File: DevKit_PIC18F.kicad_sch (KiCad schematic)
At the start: 27 parts, among them J1 PIC_ICSP_ICD, J2 USB_C_Receptacle_USB2.0_16P, J4 RA_PORT, J5 RB_PORT, J6 RD_PORT, J7 RC_PORT, J8 RE_PORT, J9 2P_UART, SW1 SW_DIP, X1 16MHz

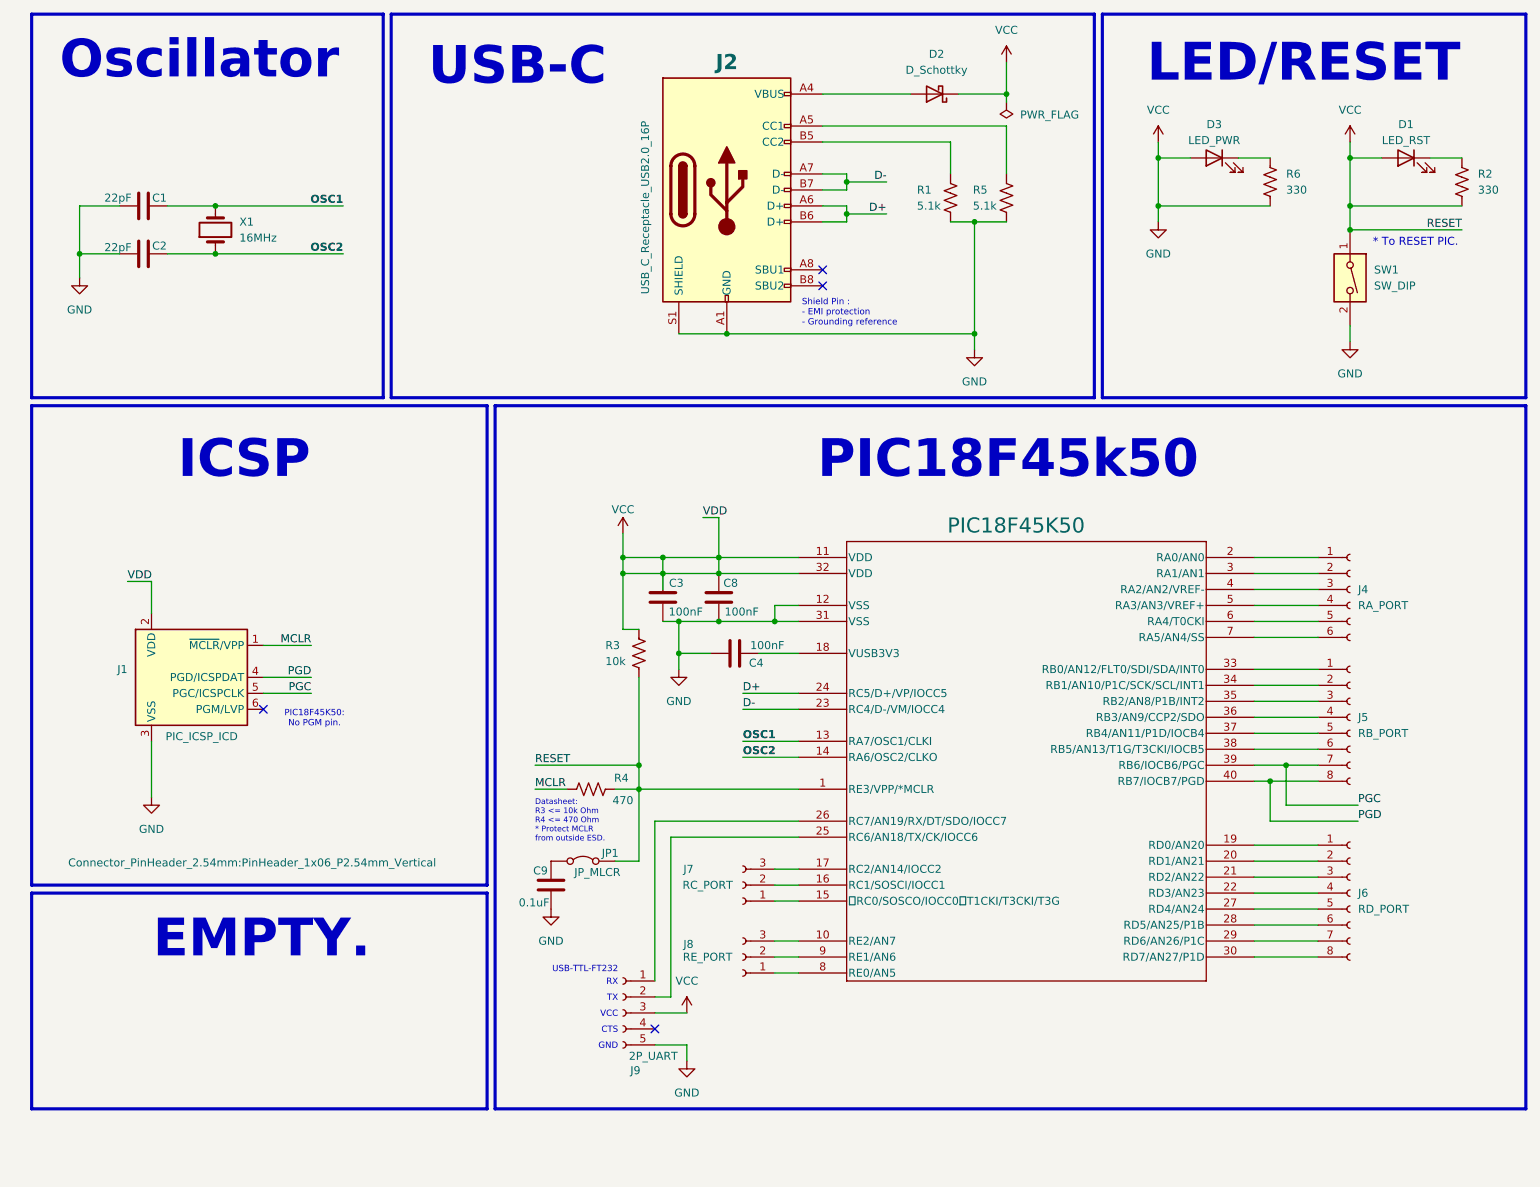
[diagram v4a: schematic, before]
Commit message: Added ICSP LED, D+/- tuned length, Cap placement/footprint update.
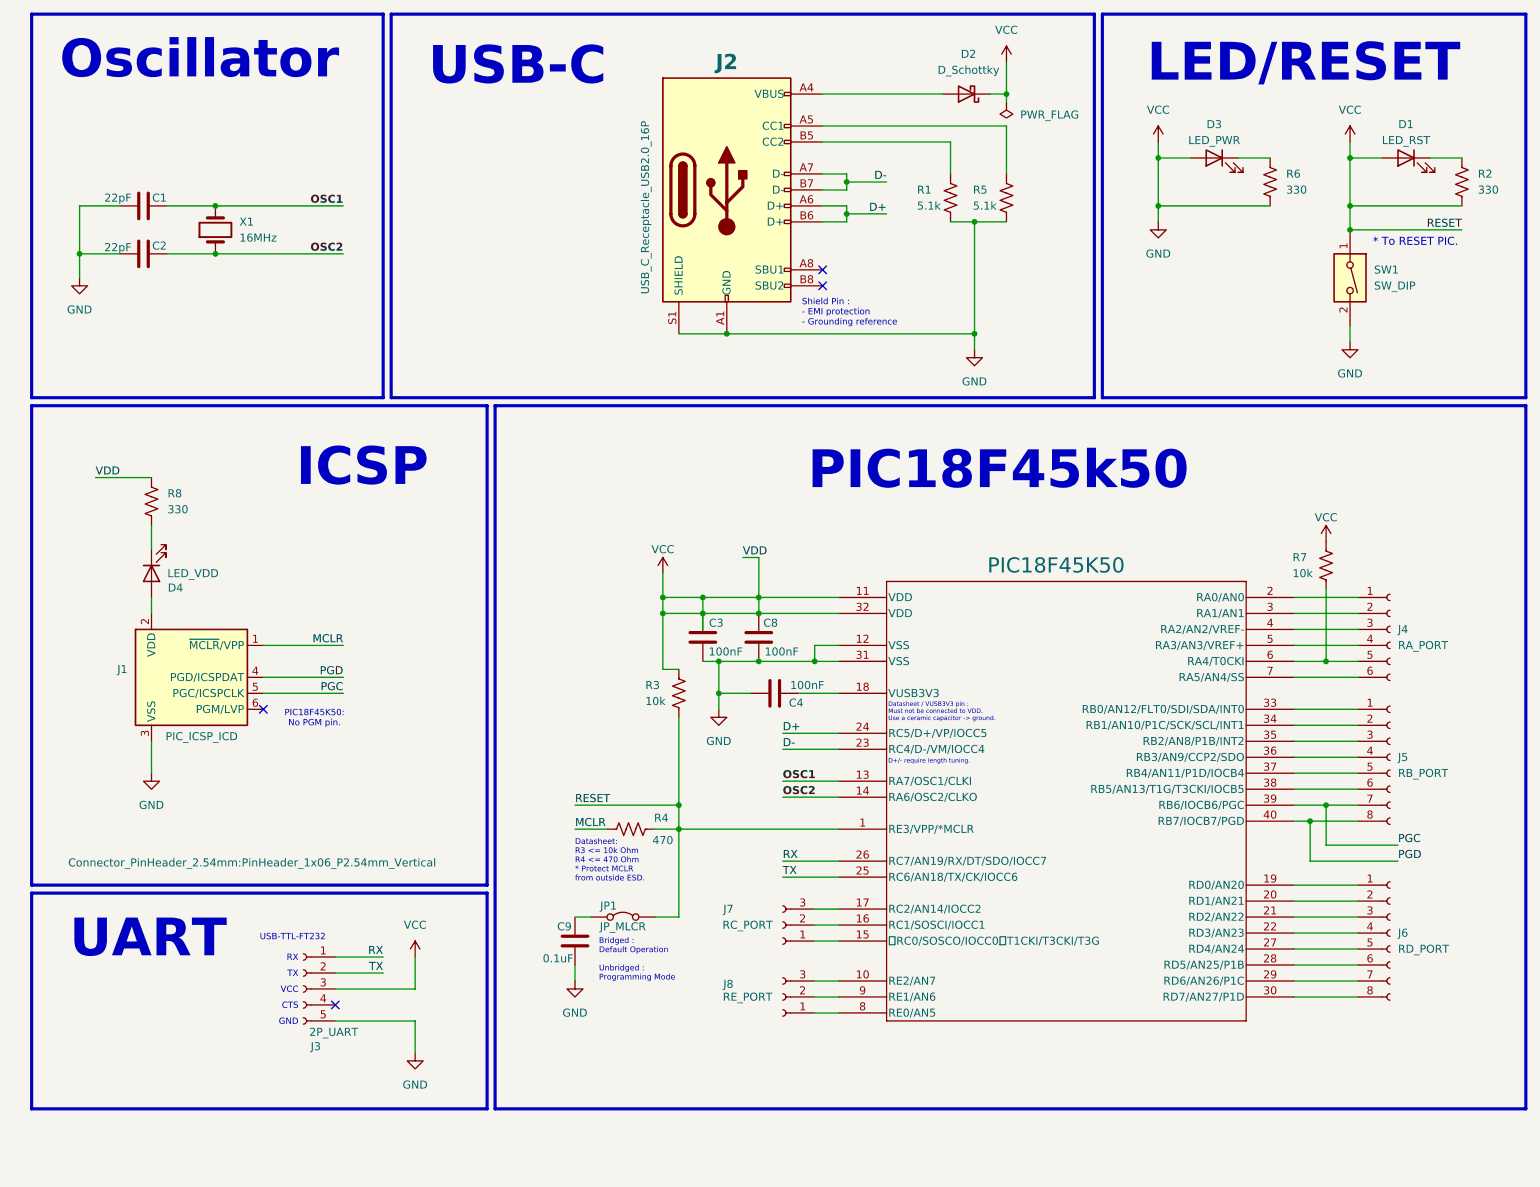
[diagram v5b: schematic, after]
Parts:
- removed J9: 2P_UART, Connector_PinSocket_2.54mm:PinSocket_1x05_P2.54mm_Vertical, symbol Connector:Conn_01x05_Socket
- added D4: LED_VDD, LED_THT:LED_D3.0mm_FlatTop, symbol Device:LED
- added J3: 2P_UART, Connector_PinSocket_2.54mm:PinSocket_1x05_P2.54mm_Vertical, symbol Connector:Conn_01x05_Socket
- added R7: 10k, Resistor_THT:R_Axial_DIN0204_L3.6mm_D1.6mm_P5.08mm_Horizontal, symbol Device:R_US
- added R8: 330, Resistor_THT:R_Axial_DIN0204_L3.6mm_D1.6mm_P5.08mm_Horizontal, symbol Device:R_US
- C4, C9: footprint Capacitor_THT:CP_Radial_D4.0mm_P2.00mm -> Capacitor_THT:C_Disc_D3.0mm_W1.6mm_P2.50mm
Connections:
- net GND: now also J3.3 (Pin_3), J3.5 (Pin_5), R7.1, R8.1; no longer J1.2 (VDD)
- net RX: now reaches PIC18F45K50.26 (RC7/AN19/RX/DT/SDO/IOCC7)
- net RX: now also J3.1 (Pin_1)
- net TX: now reaches PIC18F45K50.25 (RC6/AN18/TX/CK/IOCC6)
- net TX: now also J3.2 (Pin_2)
- net at J4.5 (Pin_5), PIC18F45K50.6 (RA4/T0CKI): now also R7.2
- new net: D4.1 (K), R8.2
- new net: D4.2 (A), J1.2 (VDD)
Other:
- note added: "Bridged : Default Operation Unbridged : Programming Mode"
- note added: "D+/- require length tuning."
- note added: "Datasheet / VUSB3V3 pin : Must not be connected to VDD. Use a ceramic capacitor -> ground."
- note added: "UART"
- note removed: "EMPTY."
- moved on the sheet: C3, C4, C8, C9, D2, J4, J5, J6, J7, J8, JP1, PIC18F45K50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

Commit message: Add LED/Diode-S->ICSP.
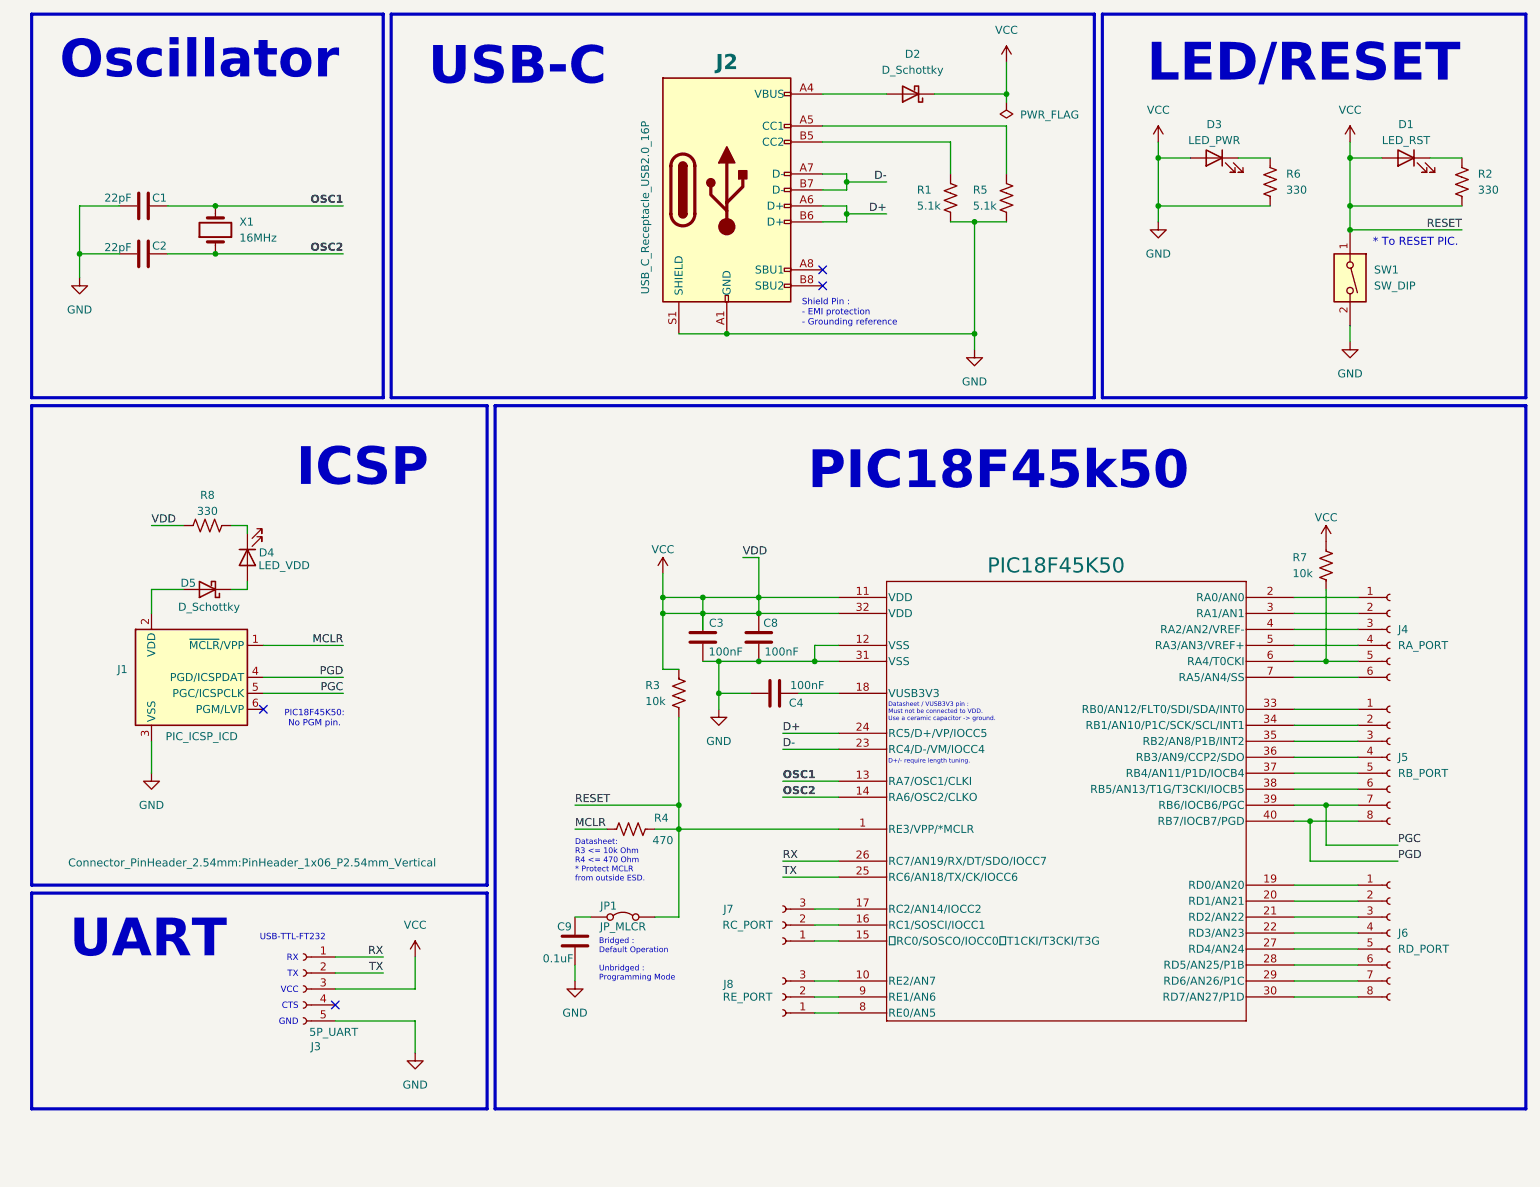
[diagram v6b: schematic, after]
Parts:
- added D5: D_Schottky, Diode_THT:D_DO-34_SOD68_P7.62mm_Horizontal, symbol Device:D_Schottky
- J3: value 2P_UART -> 5P_UART
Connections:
- net at D4.2 (A): now also D5.1 (K); no longer J1.2 (VDD)
- new net: D5.2 (A), J1.2 (VDD)
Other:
- moved on the sheet: D2, D4, R8
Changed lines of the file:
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@@
 	(wire
 		(pts
+			(xy 48.26 93.98) (xy 48.26 95.25)
+		)
+		(stroke
+			(width 0)
+			(type default)
+		)
+	)
+	(wire
+		(pts
 			(xy 224.79 135.89) (xy 214.63 135.89)
 		)
@@
 	(wire
 		(pts
-			(xy 168.91 25.4) (xy 166.37 25.4)
+			(xy 168.91 25.4) (xy 157.48 25.4)
 		)
 		(stroke
@@
 	(wire
 		(pts
-			(xy 33.02 105.41) (xy 33.02 107.95)
-		)
-		(stroke
-			(width 0)
-			(type default)
-		)
-	)
-	(wire
-		(pts
 			(xy 163.83 66.04) (xy 163.83 63.5)
 		)
@@
 	(wire
 		(pts
+			(xy 48.26 104.14) (xy 45.72 104.14)
+		)
+		(stroke
+			(width 0)
+			(type default)
+		)
+	)
+	(wire
+		(pts
 			(xy 116.84 142.24) (xy 142.24 142.24)
 		)
@@
 	(wire
 		(pts
-			(xy 24.13 86.36) (xy 33.02 86.36)
+			(xy 33.02 93.98) (xy 38.1 93.98)
 		)
 		(stroke
@@
 	(wire
 		(pts
+			(xy 33.02 104.14) (xy 33.02 107.95)
+		)
+		(stroke
+			(width 0)
+			(type default)
+		)
+	)
+	(wire
+		(pts
 			(xy 100.33 138.43) (xy 116.84 138.43)
 		)
@@
 	(wire
 		(pts
-			(xy 224.79 125.73) (xy 214.63 125.73)
+			(xy 38.1 104.14) (xy 33.02 104.14)
 		)
 		(stroke
@@
 	(wire
 		(pts
-			(xy 116.84 124.46) (xy 116.84 138.43)
+			(xy 224.79 125.73) (xy 214.63 125.73)
 		)
 		(stroke
@@
 	(wire
 		(pts
-			(xy 139.7 30.48) (xy 168.91 30.48)
+			(xy 116.84 124.46) (xy 116.84 138.43)
 		)
 		(stroke
@@
 	(wire
 		(pts
-			(xy 133.35 149.86) (xy 142.24 149.86)
+			(xy 139.7 30.48) (xy 168.91 30.48)
 		)
 		(stroke
@@
 	(wire
 		(pts
-			(xy 143.51 43.18) (xy 143.51 44.45)
+			(xy 133.35 149.86) (xy 142.24 149.86)
 		)
 		(stroke
@@
 	(wire
 		(pts
-			(xy 123.19 120.65) (xy 128.27 120.65)
+			(xy 143.51 43.18) (xy 143.51 44.45)
 		)
 		(stroke
@@
 	(wire
 		(pts
-			(xy 133.35 127) (xy 142.24 127)
+			(xy 123.19 120.65) (xy 128.27 120.65)
 		)
 		(stroke
@@
 	(wire
 		(pts
-			(xy 114.3 107.95) (xy 114.3 116.84)
+			(xy 133.35 127) (xy 142.24 127)
 		)
 		(stroke
@@
 	(wire
 		(pts
-			(xy 33.02 93.98) (xy 33.02 97.79)
+			(xy 114.3 107.95) (xy 114.3 116.84)
 		)
 		(stroke
@@
 	(wire
 		(pts
+			(xy 48.26 102.87) (xy 48.26 104.14)
+		)
+		(stroke
+			(width 0)
+			(type default)
+		)
+	)
+	(wire
+		(pts
 			(xy 123.19 115.57) (xy 129.54 115.57)
 		)
@@
 	(wire
 		(pts
-			(xy 139.7 25.4) (xy 158.75 25.4)
+			(xy 139.7 25.4) (xy 149.86 25.4)
 		)
 		(stroke
@@
 	(wire
 		(pts
+			(xy 45.72 93.98) (xy 48.26 93.98)
+		)
+		(stroke
+			(width 0)
+			(type default)
+		)
+	)
+	(wire
+		(pts
 			(xy 224.79 140.97) (xy 217.17 140.97)
 		)
@@
 	)
 	(label "VDD"
-		(at 24.13 86.36 0)
+		(at 33.02 93.98 0)
 		(fields_autoplaced yes)
 		(effects
@@
 	)
 	(symbol
+		(lib_id "Device:D_Schottky")
+		(at 41.91 104.14 180)
+		(unit 1)
+		(exclude_from_sim no)
+		(in_bom yes)
+		(on_board yes)
+		(dnp no)
+		(property "Reference" "D5"
+			(at 38.862 103.124 0)
+			(effects
+				(font
+					(size 1.27 1.27)
+				)
+			)
+		)
+		(property "Value" "D_Schottky"
+			(at 42.164 106.934 0)
+			(effects
+				(font
+					(size 1.27 1.27)
+				)
+			)
+		)
+		(property "Footprint" "Diode_THT:D_DO-34_SOD68_P7.62mm_Horizontal"
+			(at 41.91 104.14 0)
+			(effects
+				(font
+					(size 1.27 1.27)
+				)
+				(hide yes)
+			)
+		)
+		(property "Datasheet" "~"
+			(at 41.91 104.14 0)
+			(effects
+				(font
+					(size 1.27 1.27)
+				)
+				(hide yes)
+			)
+		)
+		(property "Description" "Schottky diode"
+			(at 41.91 104.14 0)
+			(effects
+				(font
+					(size 1.27 1.27)
+				)
+				(hide yes)
+			)
+		)
+		(pin "1"
+		)
+		(pin "2"
+		)
+		(instances
+			(project "DevKit_PIC18F"
+				(path "/495af0d8-3788-4f6a-8ee9-f4c61668daf8"
+					(reference "D5")
+					(unit 1)
+				)
+			)
+		)
+	)
+	(symbol
 		(lib_id "power:VCC")
 		(at 193.04 33.02 0)
@@
 			)
 		)
-		(property "Value" "2P_UART"
+		(property "Value" "5P_UART"
 			(at 61.976 174.498 0)
 			(effects
@@
 	(symbol
 		(lib_id "Device:R_US")
-		(at 33.02 90.17 0)
+		(at 41.91 93.98 90)
 		(unit 1)
 		(exclude_from_sim no)
@@
 		(on_board yes)
 		(dnp no)
-		(fields_autoplaced yes)
 		(property "Reference" "R8"
-			(at 35.56 88.8999 0)
+			(at 41.91 89.154 90)
 			(effects
 				(font
 					(size 1.27 1.27)
 				)
-				(justify left)
 			)
 		)
 		(property "Value" "330"
-			(at 35.56 91.4399 0)
+			(at 41.91 91.694 90)
 			(effects
 				(font
 					(size 1.27 1.27)
 				)
-				(justify left)
 			)
 		)
 		(property "Footprint" "Resistor_THT:R_Axial_DIN0204_L3.6mm_D1.6mm_P5.08mm_Horizontal"
-			(at 34.036 90.424 90)
+			(at 42.164 92.964 90)
 			(effects
 				(font
@@
 		)
 		(property "Datasheet" "~"
-			(at 33.02 90.17 0)
+			(at 41.91 93.98 0)
 			(effects
 				(font
@@
 		)
 		(property "Description" "Resistor, US symbol"
-			(at 33.02 90.17 0)
+			(at 41.91 93.98 0)
 			(effects
 				(font
@@
 	(symbol
 		(lib_id "Device:LED")
-		(at 33.02 101.6 90)
+		(at 48.26 99.06 90)
 		(mirror x)
 		(unit 1)
@@
 		(dnp no)
 		(property "Reference" "D4"
-			(at 36.83 103.886 90)
+			(at 51.308 98.298 90)
 			(effects
 				(font
@@
 		)
 		(property "Value" "LED_VDD"
-			(at 39.624 101.6 90)
+			(at 54.102 100.33 90)
 			(effects
 				(font
@@
 		)
 		(property "Footprint" "LED_THT:LED_D3.0mm_FlatTop"
-			(at 33.02 101.6 0)
+			(at 48.26 99.06 0)
 			(effects
 				(font
@@
 		)
 		(property "Datasheet" "~"
-			(at 33.02 101.6 0)
+			(at 48.26 99.06 0)
 			(effects
 				(font
@@
 		)
 		(property "Description" "Light emitting diode"
-			(at 33.02 101.6 0)
+			(at 48.26 99.06 0)
 			(effects
 				(font
@@
 	(symbol
 		(lib_id "Device:D_Schottky")
-		(at 162.56 25.4 180)
+		(at 153.67 25.4 180)
 		(unit 1)
 		(exclude_from_sim no)
@@
 		(fields_autoplaced yes)
 		(property "Reference" "D2"
-			(at 162.8775 19.05 0)
+			(at 153.9875 19.05 0)
 			(effects
 				(font
@@
 		)
 		(property "Value" "D_Schottky"
-			(at 162.8775 21.59 0)
+			(at 153.9875 21.59 0)
 			(effects
 				(font
@@
 		)
 		(property "Footprint" "Diode_THT:D_DO-34_SOD68_P7.62mm_Horizontal"
-			(at 162.56 25.4 0)
+			(at 153.67 25.4 0)
 			(effects
 				(font
@@
 		)
 		(property "Datasheet" "~"
-			(at 162.56 25.4 0)
+			(at 153.67 25.4 0)
 			(effects
 				(font
@@
 		)
 		(property "Description" "Schottky diode"
-			(at 162.56 25.4 0)
+			(at 153.67 25.4 0)
 			(effects
 				(font
